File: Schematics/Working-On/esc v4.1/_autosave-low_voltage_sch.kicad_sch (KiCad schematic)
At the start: 38 parts, among them IC1 74HCT08BQ,115, IC2 74HCT08BQ,115, U2 ATmega328P-M

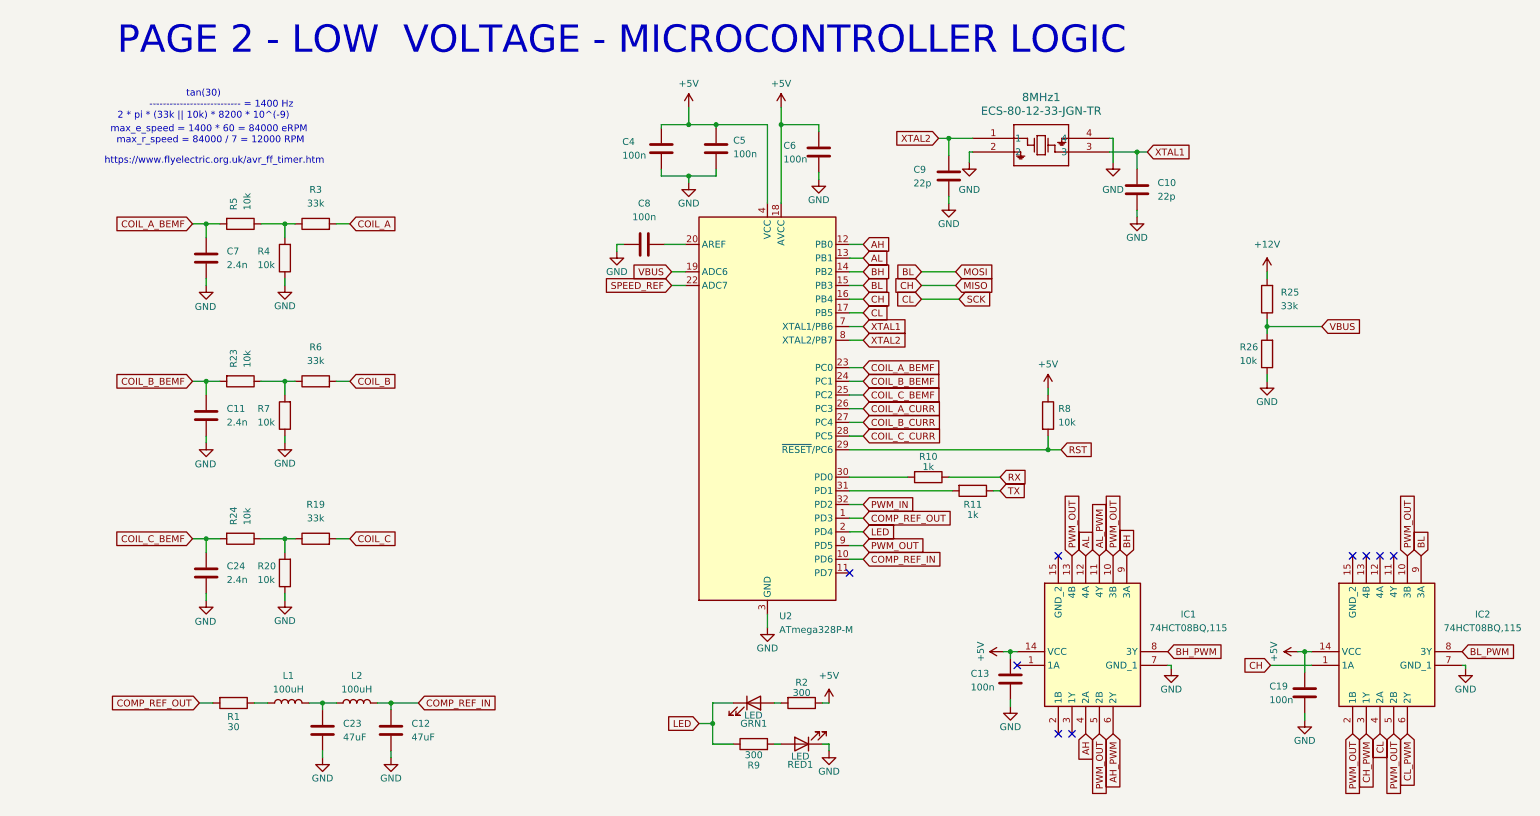
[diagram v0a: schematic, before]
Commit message: Added VBUS measurment.
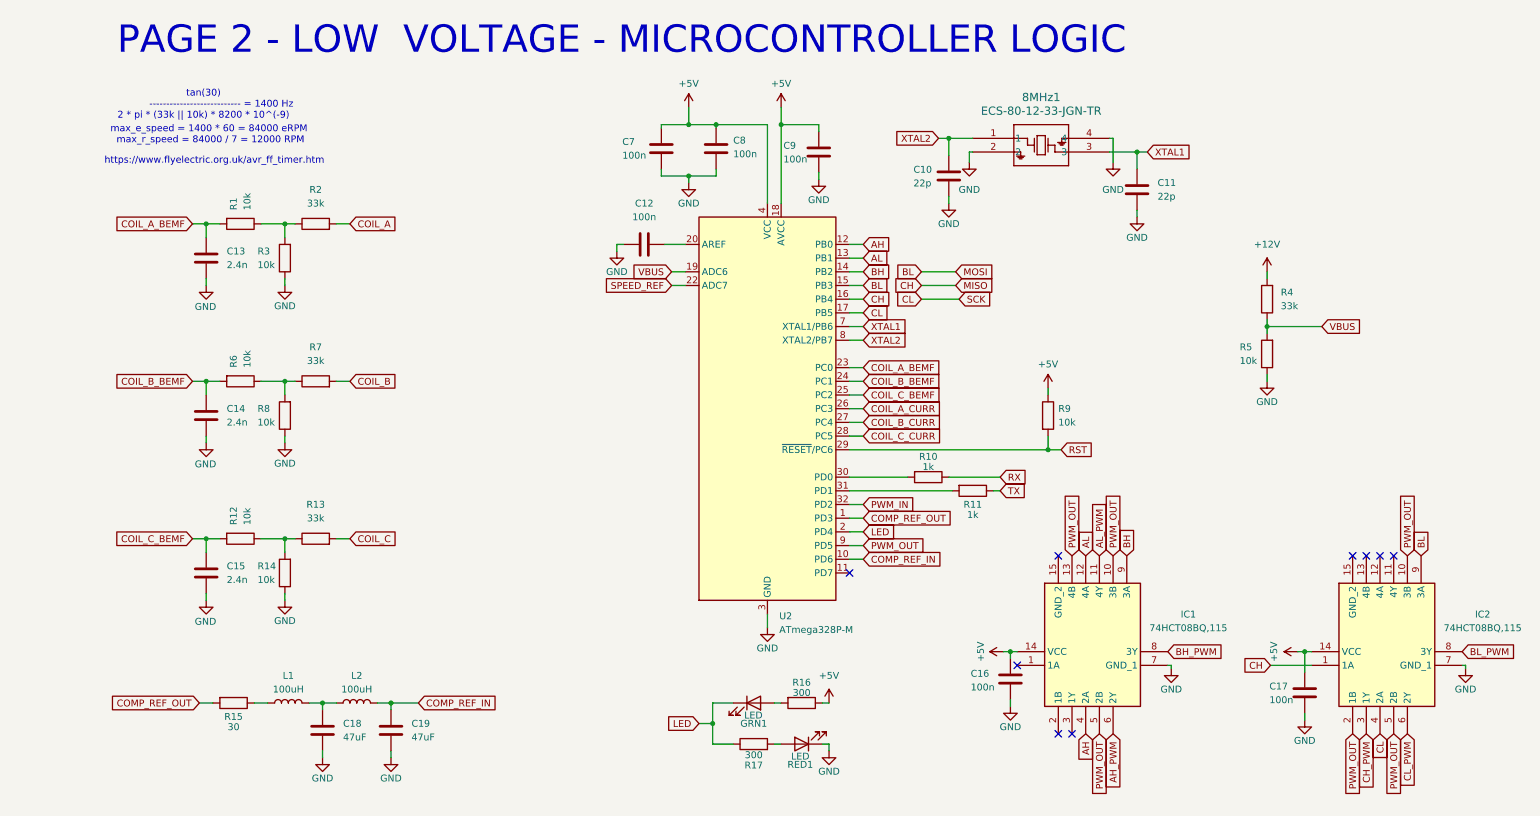
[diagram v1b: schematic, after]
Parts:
- renumbered C9 to C10, C10 to C11, C8 to C12, C7 to C13, C11 to C14, C24 to C15, C13 to C16, C19 to C17, C23 to C18, C12 to C19, C4 to C7, C5 to C8, C6 to C9, R5 to R1, R24 to R12, R19 to R13, R20 to R14, R1 to R15, R2 to R16, R9 to R17, R3 to R2, R4 to R3, R25 to R4, R26 to R5, R23 to R6, R6 to R7, R7 to R8, R8 to R9
